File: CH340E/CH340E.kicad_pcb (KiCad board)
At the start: 2 copper layers, 15.5 x 20.3 mm, 21 parts, among them J2 Conn_01x06, P1 USB_C_Plug_USB2.0, U1 CH340E, U2 AP2127K-3.3

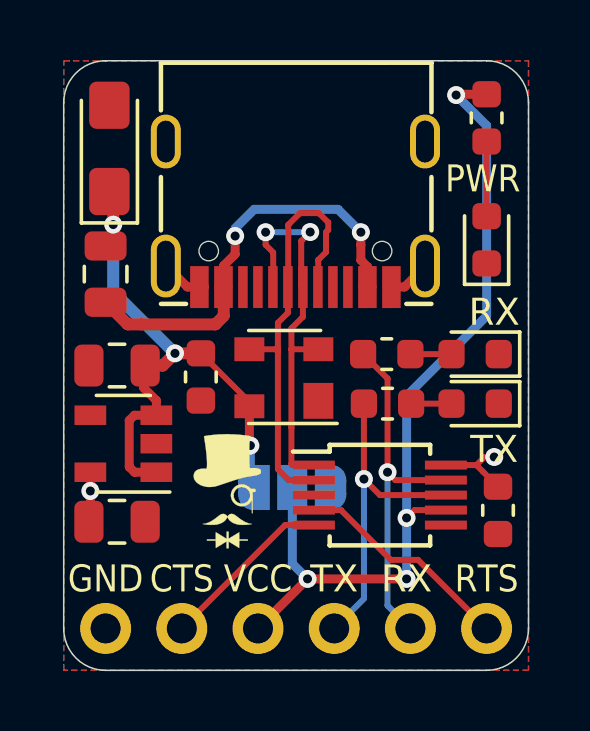
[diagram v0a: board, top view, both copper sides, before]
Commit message: Board Sizes Reduced in Width by 0.254mm
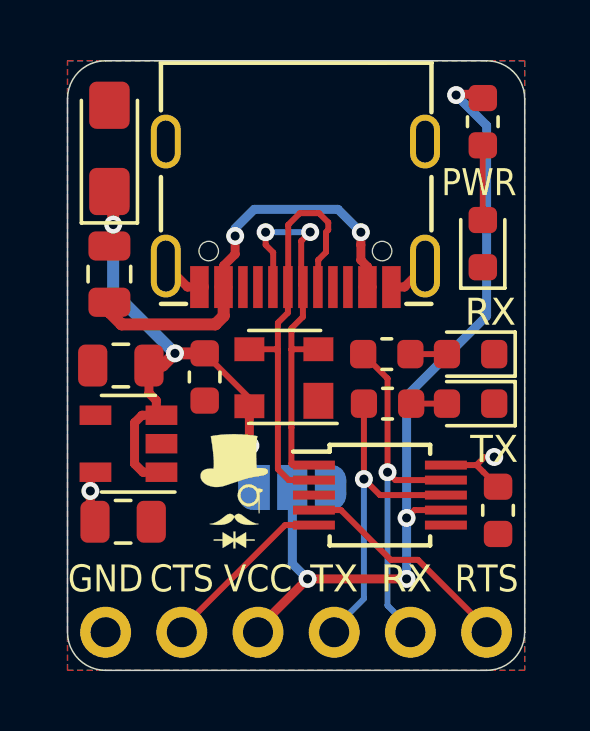
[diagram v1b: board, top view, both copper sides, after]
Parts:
- moved G*** 0.23 mm to (65.0, 43.4)
- moved C7 0.20 mm to (61.3, 44.5)
- moved PWR 0.18 mm to (73.3, 35.2)
- moved R1 0.18 mm to (73.3, 31.1)
- moved U2 0.17 mm to (61.5, 41.8)
- moved RX1 0.15 mm to (72.9, 38.9)
- moved TX2 0.15 mm to (72.9, 40.5)
- moved J2 0.13 mm to (73.4, 48.1)
- moved C4 0.13 mm to (64.0, 39.6)
- moved C6 0.13 mm to (61.2, 39.2)
- moved F1 0.13 mm to (60.8, 36.2)
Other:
- board size 15.5 x 20.3 mm -> 15.2 x 20.3 mm

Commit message: Soldermask width adjusted
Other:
- rule solder_mask_min_width: 0.1 -> 0.05
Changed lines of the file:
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@@
     (pad_drill 1)
     (pad_to_mask_clearance 0)
-    (solder_mask_min_width 0.1)
+    (solder_mask_min_width 0.05)
     (aux_axis_origin 0 0)
     (visible_elements 7FFFFFFF)
@@
     )
   )
+  (gr_arc (start 73.406 48.133) (end 73.406 49.403) (angle -90) (layer Edge.Cuts) (width 0.05))
   (gr_arc (start 73.406 30.353) (end 74.676 30.353) (angle -90) (layer Edge.Cuts) (width 0.05))
   (gr_arc (start 60.706 30.353) (end 60.706 29.083) (angle -90) (layer Edge.Cuts) (width 0.05))
-  (gr_arc (start 73.406 48.133) (end 73.406 49.403) (angle -90) (layer Edge.Cuts) (width 0.05))
   (gr_arc (start 60.706 48.133) (end 59.436 48.133) (angle -90) (layer Edge.Cuts) (width 0.05))
   (gr_text TX (at 73.66 42.037) (layer F.SilkS)
@@
     (effects (font (size 0.9 0.8) (thickness 0.12)))
   )
-  (dimension 15.494 (width 0.12) (layer Dwgs.User)
-    (gr_text "15.494 mm" (at 67.056 56.388241) (layer Dwgs.User)
+  (dimension 15.24 (width 0.12) (layer Dwgs.User)
+    (gr_text "15.240 mm" (at 67.056 56.388241) (layer Dwgs.User)
       (effects (font (size 1 1) (thickness 0.15)) hide)
     )
-    (feature1 (pts (xy 74.803 49.403) (xy 74.803 55.704662)))
-    (feature2 (pts (xy 59.309 49.403) (xy 59.309 55.704662)))
-    (crossbar (pts (xy 59.309 55.118241) (xy 74.803 55.118241)))
-    (arrow1a (pts (xy 74.803 55.118241) (xy 73.676496 55.704662)))
-    (arrow1b (pts (xy 74.803 55.118241) (xy 73.676496 54.53182)))
-    (arrow2a (pts (xy 59.309 55.118241) (xy 60.435504 55.704662)))
-    (arrow2b (pts (xy 59.309 55.118241) (xy 60.435504 54.53182)))
+    (feature1 (pts (xy 74.676 49.403) (xy 74.676 55.704662)))
+    (feature2 (pts (xy 59.436 49.403) (xy 59.436 55.704662)))
+    (crossbar (pts (xy 59.436 55.118241) (xy 74.676 55.118241)))
+    (arrow1a (pts (xy 74.676 55.118241) (xy 73.549496 55.704662)))
+    (arrow1b (pts (xy 74.676 55.118241) (xy 73.549496 54.53182)))
+    (arrow2a (pts (xy 59.436 55.118241) (xy 60.562504 55.704662)))
+    (arrow2b (pts (xy 59.436 55.118241) (xy 60.562504 54.53182)))
   )
   (dimension 12.7 (width 0.12) (layer Dwgs.User)
@@
   )
   (dimension 20.32 (width 0.12) (layer Dwgs.User)
-    (gr_text "20.320 mm" (at 54.991 39.243 90) (layer Dwgs.User)
+    (gr_text "20.320 mm" (at 55.118 39.243 90) (layer Dwgs.User)
       (effects (font (size 1 1) (thickness 0.15)) hide)
     )
-    (feature1 (pts (xy 59.309 29.083) (xy 55.674579 29.083)))
-    (feature2 (pts (xy 59.309 49.403) (xy 55.674579 49.403)))
-    (crossbar (pts (xy 56.261 49.403) (xy 56.261 29.083)))
-    (arrow1a (pts (xy 56.261 29.083) (xy 56.847421 30.209504)))
-    (arrow1b (pts (xy 56.261 29.083) (xy 55.674579 30.209504)))
-    (arrow2a (pts (xy 56.261 49.403) (xy 56.847421 48.276496)))
-    (arrow2b (pts (xy 56.261 49.403) (xy 55.674579 48.276496)))
+    (feature1 (pts (xy 59.436 29.083) (xy 55.801579 29.083)))
+    (feature2 (pts (xy 59.436 49.403) (xy 55.801579 49.403)))
+    (crossbar (pts (xy 56.388 49.403) (xy 56.388 29.083)))
+    (arrow1a (pts (xy 56.388 29.083) (xy 56.974421 30.209504)))
+    (arrow1b (pts (xy 56.388 29.083) (xy 55.801579 30.209504)))
+    (arrow2a (pts (xy 56.388 49.403) (xy 56.974421 48.276496)))
+    (arrow2b (pts (xy 56.388 49.403) (xy 55.801579 48.276496)))
   )
   (gr_text "CH340E USB - UART" (at 67.056 41.529) (layer B.SilkS)

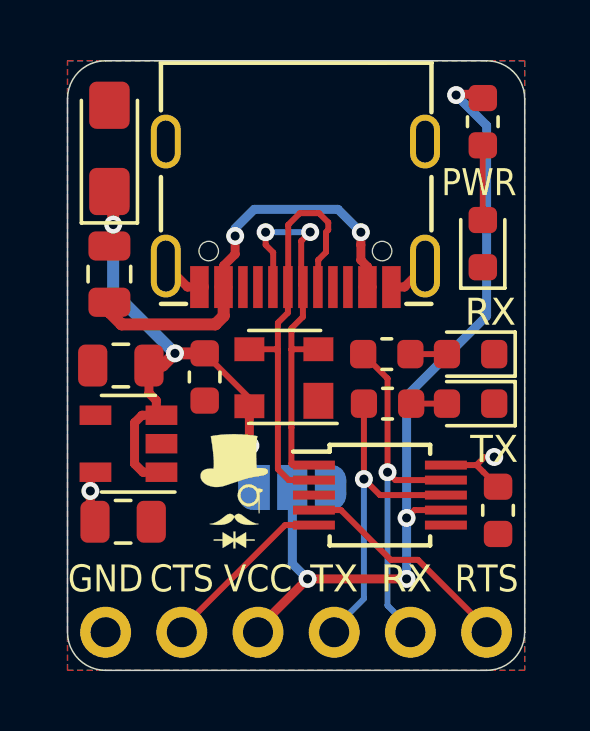
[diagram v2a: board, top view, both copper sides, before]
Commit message: CH340E Fix
5k1 Resistors added to CC1 and CC2, TX and RX LEDs pulled up to VCC,Copper Pour changed from 3V3 to VCC.
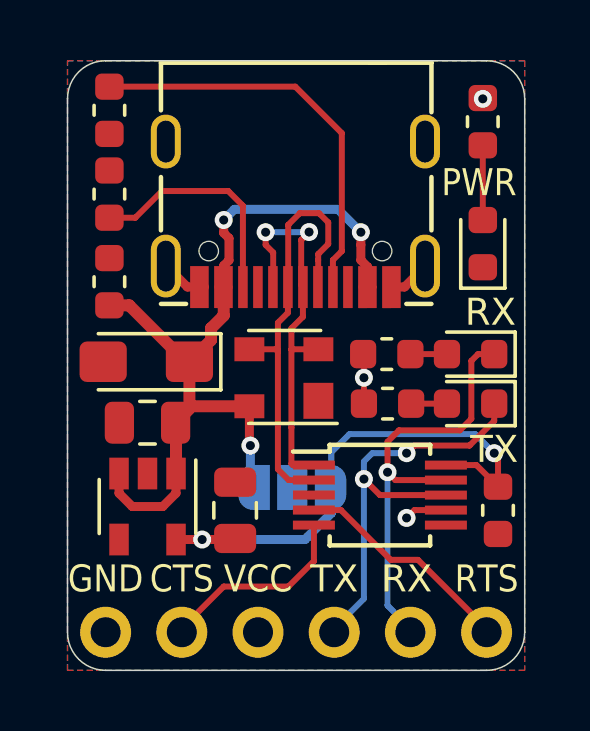
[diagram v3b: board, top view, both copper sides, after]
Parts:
- removed F1: 500mA, Resistor_SMD:R_0805_2012Metric
- removed the G*** at (65.0, 43.4)
- added R4: 5K1, Resistor_SMD:R_0603_1608Metric, F.Cu at (60.8, 33.5)
- added R5: 5K1, Resistor_SMD:R_0603_1608Metric, F.Cu at (60.8, 30.7)
- moved C3 7.22 mm to (62.1, 39.1), turned to 180 degrees
- moved C4 4.49 mm to (60.8, 36.4), turned to 90 degrees
- moved C7 3.75 mm to (65.0, 44.1), turned to 90 degrees
- moved U2 2.19 mm to (62.1, 43.9), turned to 270 degrees
- moved C6 2.10 mm to (62.1, 41.1)
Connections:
- P1 pad A4: Net-(F1-Pad2) -> VBUS
- P1 pad A9: Net-(F1-Pad2) -> VBUS
- P1 pad B4: Net-(F1-Pad2) -> VBUS
- P1 pad B9: Net-(F1-Pad2) -> VBUS
- R2 pad 1: TX -> VCC
- R3 pad 1: RX -> VCC
- RX1 pad 1: GND -> RX
- TX2 pad 1: GND -> TX
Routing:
- net VCC: track 29.0 -> 3.08 mm, vias 4 -> 3
- net Net-(F1-Pad2): track 15.5 -> 0.00 mm, vias 2 -> 0
- net Net-(P1-PadA5): track 0.00 -> 13.6 mm
- net 3V3: track 4.34 -> 17.8 mm
- net VBUS: track 19.4 -> 29.6 mm
- net Net-(P1-PadB5): track 0.00 -> 7.73 mm
- net TX: track 10.9 -> 14.4 mm, vias 1 -> 2
- net RX: track 11.9 -> 14.5 mm
- net CTS: track 5.83 -> 6.53 mm
- added copper zone on B.Cu, net VCC
- removed copper zone on B.Cu, net 3V3

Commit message: SiRUSB Updates
USB-C 3D Renders Added and Pictures Updated
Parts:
- J2: footprint Connector_PinHeader_2.54mm:PinHeader_1x06_P2.54mm_Vertical -> Connector_PinHeader_2.54mm:PinHeader_1x06_P2.54mm_Horizontal; moved to F.Cu
- turned J2 to 270 degrees

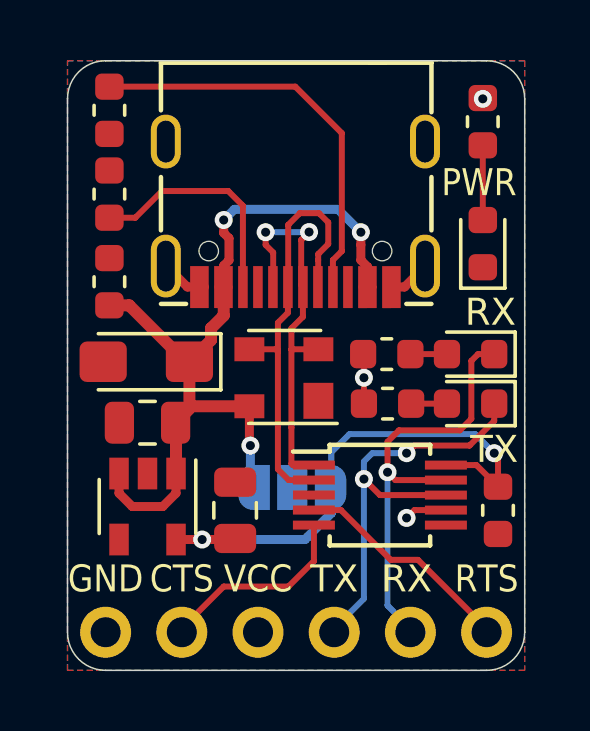
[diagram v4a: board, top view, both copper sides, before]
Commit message: SirUSB Board Revisions
Removed MicroUSB Versions of FT230 and FT231, SolderPaste Layer Adjusted to -0.05mm, Silkscreens optimised, OSHW logo added.
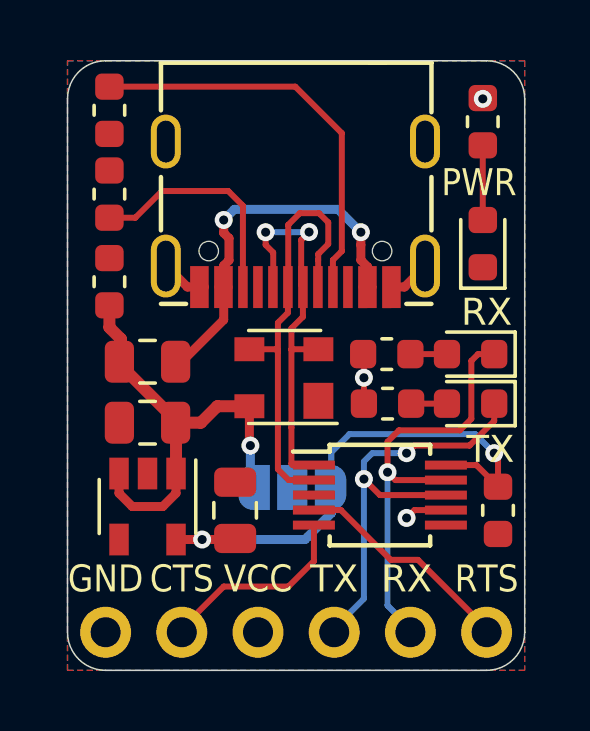
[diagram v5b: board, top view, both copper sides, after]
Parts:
- removed C3: 22uF, Capacitor_Tantalum_SMD:CP_EIA-3216-18_Kemet-A_Pad1.58x1.35mm_HandSolder
- added F1: 500mA, Fuse:Fuse_0805_2012Metric, F.Cu at (62.1, 39.1)
- added G***: LOGO, logo:OSHW36x26, B.Cu at (73.2, 33.8)
- G***: footprint logo:logo76x107 -> logo:logo63x89
- G***: footprint logo:SirBoard98x31 -> logo:SirBoard112x35
- PWR: value BLUE -> RED
- TX1: renamed from TX2; value RED -> GREEN
- moved G*** 0.10 mm to (67.1, 39.0)
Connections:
- P1 pad A4: VBUS -> Net-(F1-Pad2)
- P1 pad A9: VBUS -> Net-(F1-Pad2)
- P1 pad B4: VBUS -> Net-(F1-Pad2)
- P1 pad B9: VBUS -> Net-(F1-Pad2)
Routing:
- net Net-(F1-Pad2): track 0.00 -> 13.8 mm, vias 0 -> 2
- net VBUS: track 29.6 -> 15.9 mm, vias 3 -> 1
